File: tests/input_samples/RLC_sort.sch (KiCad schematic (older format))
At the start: 21 parts

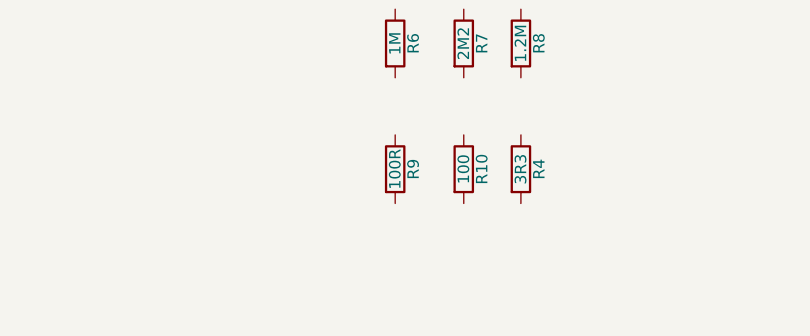
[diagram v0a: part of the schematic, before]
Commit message: Modified the sort function to recycle the code in units.py
This code is native to KiBoM and support much more cases.
I didn't know about it.

Also added a test to make sure 1M and 1m are different.
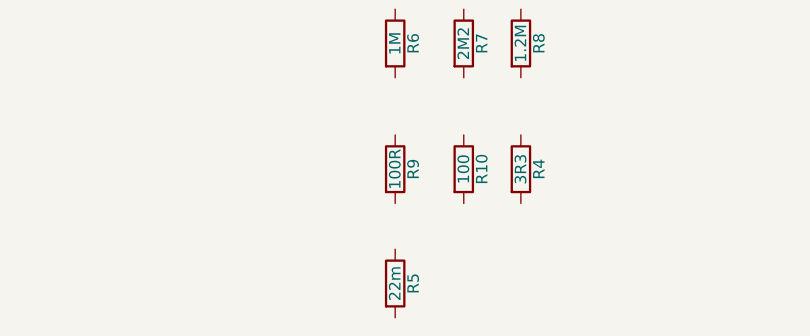
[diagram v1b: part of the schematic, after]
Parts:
- added R5: 22m, Resistor_SMD:R_0603_1608Metric, symbol Device:R
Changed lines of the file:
@@
+	1    0    0    -1
+$EndComp
+$Comp
+L Device:R R5
+U 1 1 5F10D5C6
+P 2200 4150
+F 0 "R5" V 2280 4150 50  0000 C CNN
+F 1 "22m" V 2200 4150 50  0000 C CNN
+F 2 "Resistor_SMD:R_0603_1608Metric" V 2130 4150 50  0001 C CNN
+F 3 "~" H 2200 4150 50  0001 C CNN
+	1    2200 4150
 	1    0    0    -1
 $EndComp
